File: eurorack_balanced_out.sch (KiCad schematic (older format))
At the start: 6 parts

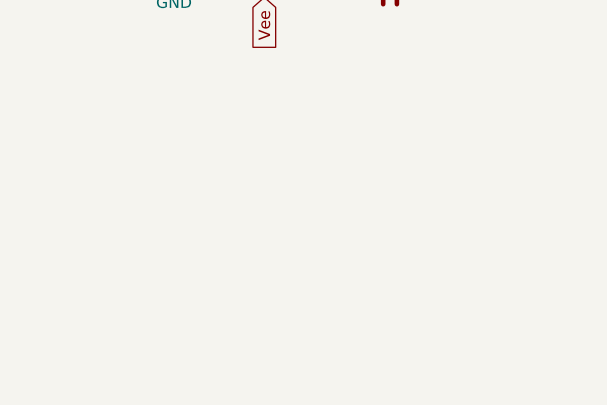
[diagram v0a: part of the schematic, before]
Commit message: add eurorack power connector + filtering
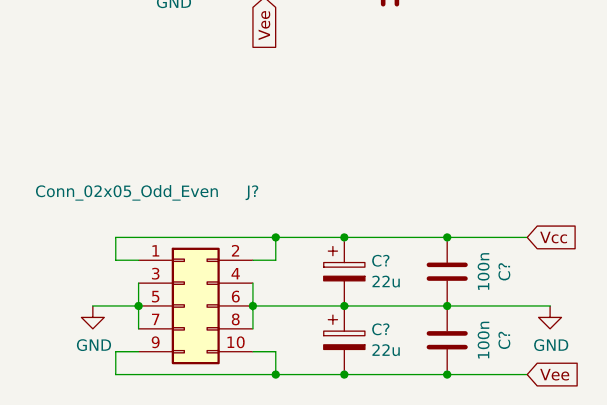
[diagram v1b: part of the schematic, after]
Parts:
- added C? (x2): 22u, Capacitor_SMD:CP_Elec_6.3x5.4, symbol Device:CP
- added C? (x2): 100n, Capacitor_SMD:C_0805_2012Metric_Pad1.15x1.40mm_HandSolder, symbol Device:C
- added J?: Conn_02x05_Odd_Even, symbol Connector_Generic:Conn_02x05_Odd_Even
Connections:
- net GND: now also C?.1, C?.1, C?.2, C?.2, J?.3 (Pin_3), J?.4 (Pin_4), J?.5 (Pin_5), J?.6 (Pin_6), J?.7 (Pin_7), J?.8 (Pin_8)
- net Vcc: now also C?.1, C?.2, J?.1 (Pin_1), J?.2 (Pin_2)
- net Vee: now also C?.1, C?.2, J?.10 (Pin_10), J?.9 (Pin_9)
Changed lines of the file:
@@
 Wire Wire Line
 	4400 3100 4600 3100
+$Comp
+L Connector_Generic:Conn_02x05_Odd_Even J?
+U 1 1 5EC6D021
+P 4450 4800
+F 0 "J?" H 4750 5300 50  0000 C CNN
+F 1 "Conn_02x05_Odd_Even" H 4200 5300 50  0000 C CNN
+F 2 "" H 4450 4800 50  0001 C CNN
+F 3 "~" H 4450 4800 50  0001 C CNN
+	1    4450 4800
+	1    0    0    -1
+$EndComp
+Wire Wire Line
+	4250 4900 4250 4800
+Connection ~ 4250 4800
+Wire Wire Line
+	4250 4800 4250 4700
+Wire Wire Line
+	4750 4700 4750 4800
+Connection ~ 4750 4800
+Wire Wire Line
+	4750 4800 4750 4900
+$Comp
+L power:GND #PWR?
+U 1 1 5EC6F187
+P 6050 4800
+F 0 "#PWR?" H 6050 4550 50  0001 C CNN
+F 1 "GND" H 6055 4627 50  0000 C CNN
+F 2 "" H 6050 4800 50  0001 C CNN
+F 3 "" H 6050 4800 50  0001 C CNN
+	1    6050 4800
+	1    0    0    -1
+$EndComp
+Wire Wire Line
+	4250 4800 4050 4800
+Wire Wire Line
+	4250 4600 4150 4600
+Wire Wire Line
+	4150 4600 4150 4500
+Wire Wire Line
+	4150 4500 4850 4500
+Wire Wire Line
+	4850 4500 4850 4600
+Wire Wire Line
+	4850 4600 4750 4600
+Wire Wire Line
+	4250 5000 4150 5000
+Wire Wire Line
+	4150 5000 4150 5100
+Wire Wire Line
+	4150 5100 4850 5100
+Wire Wire Line
+	4850 5100 4850 5000
+Wire Wire Line
+	4850 5000 4750 5000
+$Comp
+L Device:CP C?
+U 1 1 5EC72C83
+P 5150 4650
+F 0 "C?" H 5268 4696 50  0000 L CNN
+F 1 "22u" H 5268 4605 50  0000 L CNN
+F 2 "Capacitor_SMD:CP_Elec_6.3x5.4" H 5188 4500 50  0001 C CNN
+F 3 "~" H 5150 4650 50  0001 C CNN
+F 4 "647-UWT1E220MCL1B" H 5150 4650 50  0001 C CNN "Mouser"
+	1    5150 4650
+	1    0    0    -1
+$EndComp
+$Comp
+L Device:C C?
+U 1 1 5EC731D9
+P 5600 4650
+F 0 "C?" V 5348 4650 50  0000 C CNN
+F 1 "100n" V 5439 4650 50  0000 C CNN
+F 2 "Capacitor_SMD:C_0805_2012Metric_Pad1.15x1.40mm_HandSolder" H 5638 4500 50  0001 C CNN
+F 3 "~" H 5600 4650 50  0001 C CNN
+F 4 " 80-C0805C104K5RACLR" V 5600 4650 50  0001 C CNN "Mouser"
+	1    5600 4650
+	-1   0    0    1
+$EndComp
+Wire Wire Line
+	4850 4500 5150 4500
+Connection ~ 4850 4500
+Connection ~ 5150 4500
+Wire Wire Line
+	5150 4500 5600 4500
+Connection ~ 4850 5100
+Text GLabel 5950 5100 2    50   Input ~ 0
+Vee
+Text GLabel 5950 4500 2    50   Input ~ 0
+Vcc
+Wire Wire Line
+	5950 4500 5600 4500
+Connection ~ 5600 4500
+Connection ~ 5150 4800
+Wire Wire Line
+	5150 4800 5600 4800
+Connection ~ 5600 4800
+Wire Wire Line
+	5600 4800 6050 4800
+Wire Wire Line
+	4850 5100 5150 5100
+$Comp
+L Device:CP C?
+U 1 1 5EC7F6E5
+P 5150 4950
+F 0 "C?" H 5268 4996 50  0000 L CNN
+F 1 "22u" H 5268 4905 50  0000 L CNN
+F 2 "Capacitor_SMD:CP_Elec_6.3x5.4" H 5188 4800 50  0001 C CNN
+F 3 "~" H 5150 4950 50  0001 C CNN
+F 4 "647-UWT1E220MCL1B" H 5150 4950 50  0001 C CNN "Mouser"
+	1    5150 4950
+	1    0    0    -1
+$EndComp
+Connection ~ 5150 5100
+Wire Wire Line
+	4750 4800 5150 4800
+$Comp
+L power:GND #PWR?
+U 1 1 5EC7FEB8
+P 4050 4800
+F 0 "#PWR?" H 4050 4550 50  0001 C CNN
+F 1 "GND" H 4055 4627 50  0000 C CNN
+F 2 "" H 4050 4800 50  0001 C CNN
+F 3 "" H 4050 4800 50  0001 C CNN
+	1    4050 4800
+	1    0    0    -1
+$EndComp
+Wire Wire Line
+	5150 5100 5600 5100
+$Comp
+L Device:C C?
+U 1 1 5EC8D523
+P 5600 4950
+F 0 "C?" V 5348 4950 50  0000 C CNN
+F 1 "100n" V 5439 4950 50  0000 C CNN
+F 2 "Capacitor_SMD:C_0805_2012Metric_Pad1.15x1.40mm_HandSolder" H 5638 4800 50  0001 C CNN
+F 3 "~" H 5600 4950 50  0001 C CNN
+F 4 " 80-C0805C104K5RACLR" V 5600 4950 50  0001 C CNN "Mouser"
+	1    5600 4950
+	-1   0    0    1
+$EndComp
+Connection ~ 5600 5100
+Wire Wire Line
+	5600 5100 5950 5100
 $EndSCHEMATC

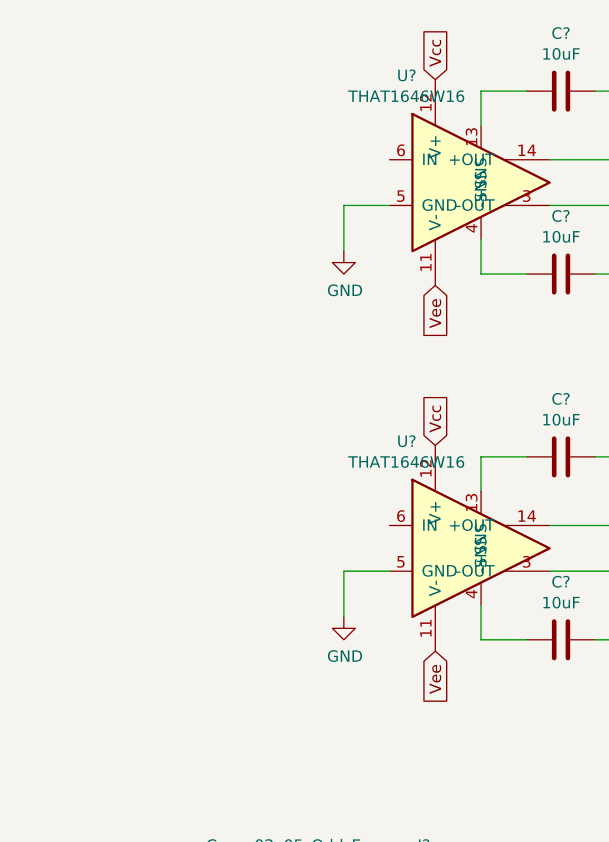
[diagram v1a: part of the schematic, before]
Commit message: add input connectors
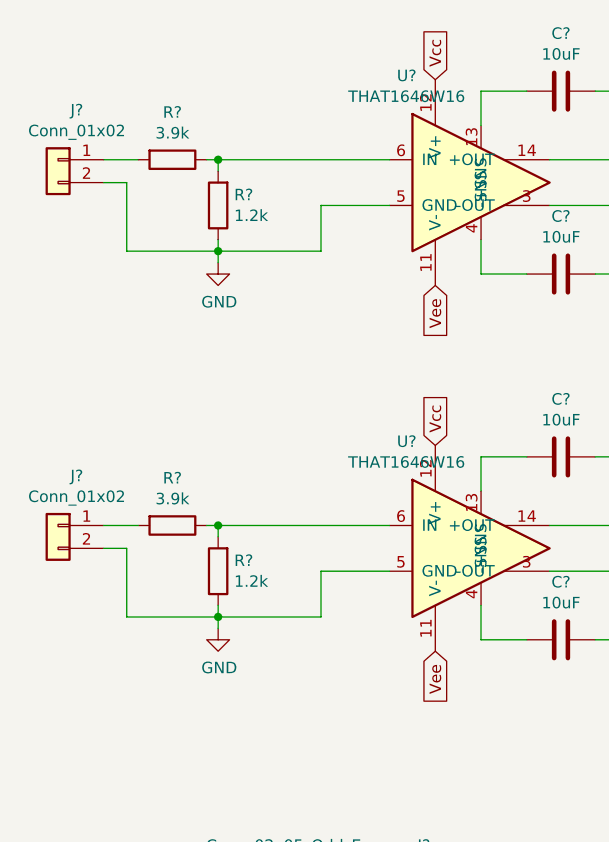
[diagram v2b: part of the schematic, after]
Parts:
- added J? (x2): Conn_01x02, symbol Connector_Generic:Conn_01x02
- added R? (x2): 3.9k, Resistor_SMD:R_0805_2012Metric_Pad1.15x1.40mm_HandSolder, symbol Device:R
- added R? (x2): 1.2k, Resistor_SMD:R_0805_2012Metric_Pad1.15x1.40mm_HandSolder, symbol Device:R
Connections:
- net GND: now also J?.2 (Pin_2), J?.2 (Pin_2), R?.1, R?.1
- net at U?.6 (IN): now also R?.1, R?.2 (x2)
- new net: J?.1 (Pin_1), R?.2 (x2)
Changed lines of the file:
@@
 L power:GND #PWR?
 U 1 1 5EC6D54F
-P 4400 1700
-F 0 "#PWR?" H 4400 1450 50  0001 C CNN
-F 1 "GND" H 4405 1527 50  0000 C CNN
-F 2 "" H 4400 1700 50  0001 C CNN
-F 3 "" H 4400 1700 50  0001 C CNN
-	1    4400 1700
-	1    0    0    -1
-$EndComp
-Wire Wire Line
-	4400 1700 4400 1500
-Wire Wire Line
-	4400 1500 4600 1500
+P 3850 1750
+F 0 "#PWR?" H 3850 1500 50  0001 C CNN
+F 1 "GND" H 3855 1577 50  0000 C CNN
+F 2 "" H 3850 1750 50  0001 C CNN
+F 3 "" H 3850 1750 50  0001 C CNN
+	1    3850 1750
+	1    0    0    -1
+$EndComp
 $Comp
 L patchut:THAT1646W16 U?
@@
 Vcc
 $Comp
-L power:GND #PWR?
-U 1 1 5EC6EB3D
-P 4400 3300
-F 0 "#PWR?" H 4400 3050 50  0001 C CNN
-F 1 "GND" H 4405 3127 50  0000 C CNN
-F 2 "" H 4400 3300 50  0001 C CNN
-F 3 "" H 4400 3300 50  0001 C CNN
-	1    4400 3300
-	1    0    0    -1
-$EndComp
-Wire Wire Line
-	4400 3300 4400 3100
-Wire Wire Line
-	4400 3100 4600 3100
-$Comp
 L Connector_Generic:Conn_02x05_Odd_Even J?
 U 1 1 5EC6D021
@@
 Wire Wire Line
 	5600 5100 5950 5100
+$Comp
+L Connector_Generic:Conn_01x02 J?
+U 1 1 5EC8DDA9
+P 3150 1300
+F 0 "J?" H 3068 1517 50  0000 C CNN
+F 1 "Conn_01x02" H 3068 1426 50  0000 C CNN
+F 2 "" H 3150 1300 50  0001 C CNN
+F 3 "~" H 3150 1300 50  0001 C CNN
+	1    3150 1300
+	-1   0    0    -1
+$EndComp
+$Comp
+L Device:R R?
+U 1 1 5EC8E9B6
+P 3650 1300
+F 0 "R?" V 3443 1300 50  0000 C CNN
+F 1 "3.9k" V 3534 1300 50  0000 C CNN
+F 2 "Resistor_SMD:R_0805_2012Metric_Pad1.15x1.40mm_HandSolder" V 3580 1300 50  0001 C CNN
+F 3 "~" H 3650 1300 50  0001 C CNN
+	1    3650 1300
+	0    1    1    0
+$EndComp
+Wire Wire Line
+	3500 1300 3350 1300
+Wire Wire Line
+	3800 1300 3850 1300
+Wire Wire Line
+	3850 1350 3850 1300
+Connection ~ 3850 1300
+Wire Wire Line
+	3850 1300 4600 1300
+Wire Wire Line
+	3850 1650 3850 1700
+Connection ~ 3850 1700
+Wire Wire Line
+	3850 1700 3850 1750
+Wire Wire Line
+	3350 1400 3450 1400
+Wire Wire Line
+	3450 1400 3450 1700
+Wire Wire Line
+	3450 1700 3850 1700
+Wire Wire Line
+	4600 1500 4300 1500
+Wire Wire Line
+	4300 1500 4300 1700
+Wire Wire Line
+	3850 1700 4300 1700
+$Comp
+L power:GND #PWR?
+U 1 1 5ECB48AD
+P 3850 3350
+F 0 "#PWR?" H 3850 3100 50  0001 C CNN
+F 1 "GND" H 3855 3177 50  0000 C CNN
+F 2 "" H 3850 3350 50  0001 C CNN
+F 3 "" H 3850 3350 50  0001 C CNN
+	1    3850 3350
+	1    0    0    -1
+$EndComp
+$Comp
+L Connector_Generic:Conn_01x02 J?
+U 1 1 5ECB48B3
+P 3150 2900
+F 0 "J?" H 3068 3117 50  0000 C CNN
+F 1 "Conn_01x02" H 3068 3026 50  0000 C CNN
+F 2 "" H 3150 2900 50  0001 C CNN
+F 3 "~" H 3150 2900 50  0001 C CNN
+	1    3150 2900
+	-1   0    0    -1
+$EndComp
+Wire Wire Line
+	3500 2900 3350 2900
+Wire Wire Line
+	3800 2900 3850 2900
+Wire Wire Line
+	3850 2950 3850 2900
+Connection ~ 3850 2900
+Wire Wire Line
+	3850 2900 4600 2900
+Wire Wire Line
+	3850 3250 3850 3300
+Connection ~ 3850 3300
+Wire Wire Line
+	3850 3300 3850 3350
+Wire Wire Line
+	3350 3000 3450 3000
+Wire Wire Line
+	3450 3000 3450 3300
+Wire Wire Line
+	3450 3300 3850 3300
+Wire Wire Line
+	3850 3300 4300 3300
+Wire Wire Line
+	4300 3300 4300 3100
+Wire Wire Line
+	4300 3100 4600 3100
+$Comp
+L Device:R R?
+U 1 1 5ECB87DC
+P 3850 1500
+F 0 "R?" H 3780 1454 50  0000 R CNN
+F 1 "1.2k" H 3780 1545 50  0000 R CNN
+F 2 "Resistor_SMD:R_0805_2012Metric_Pad1.15x1.40mm_HandSolder" V 3780 1500 50  0001 C CNN
+F 3 "~" H 3850 1500 50  0001 C CNN
+	1    3850 1500
+	-1   0    0    1
+$EndComp
+$Comp
+L Device:R R?
+U 1 1 5ECB902C
+P 3850 3100
+F 0 "R?" H 3780 3054 50  0000 R CNN
+F 1 "1.2k" H 3780 3145 50  0000 R CNN
+F 2 "Resistor_SMD:R_0805_2012Metric_Pad1.15x1.40mm_HandSolder" V 3780 3100 50  0001 C CNN
+F 3 "~" H 3850 3100 50  0001 C CNN
+	1    3850 3100
+	-1   0    0    1
+$EndComp
+$Comp
+L Device:R R?
+U 1 1 5ECB9314
+P 3650 2900
+F 0 "R?" V 3443 2900 50  0000 C CNN
+F 1 "3.9k" V 3534 2900 50  0000 C CNN
+F 2 "Resistor_SMD:R_0805_2012Metric_Pad1.15x1.40mm_HandSolder" V 3580 2900 50  0001 C CNN
+F 3 "~" H 3650 2900 50  0001 C CNN
+	1    3650 2900
+	0    1    1    0
+$EndComp
 $EndSCHEMATC

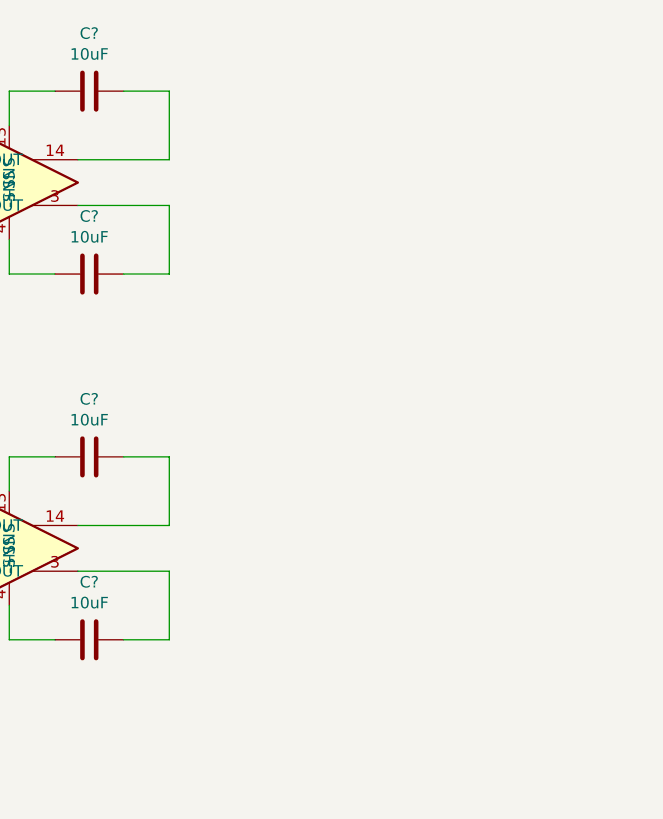
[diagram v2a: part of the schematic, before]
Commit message: add output jacks
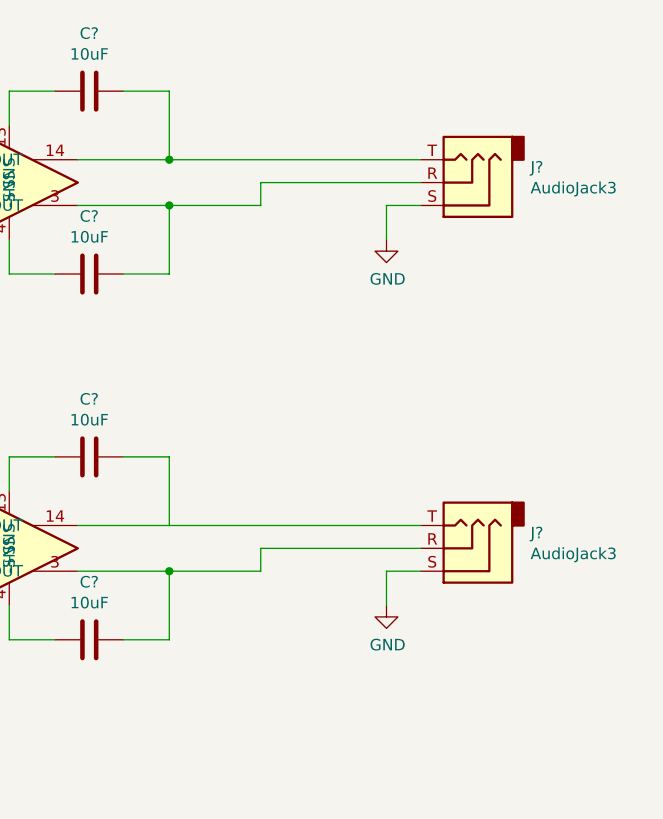
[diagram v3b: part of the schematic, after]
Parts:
- added J? (x2): AudioJack3, symbol Connector:AudioJack3
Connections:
- net GND: now also J?.S, J?.S
- net at C?.1, U?.14 (+OUT): now also J?.T (x2)
- net at C?.1, U?.3 (-OUT): now also J?.R (x2)
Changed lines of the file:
@@
 	0    1    1    0
 $EndComp
+$Comp
+L Connector:AudioJack3 J?
+U 1 1 5ECBA746
+P 7000 1400
+F 0 "J?" H 6720 1333 50  0000 R CNN
+F 1 "AudioJack3" H 6720 1424 50  0000 R CNN
+F 2 "" H 7000 1400 50  0001 C CNN
+F 3 "~" H 7000 1400 50  0001 C CNN
+	1    7000 1400
+	-1   0    0    1
+$EndComp
+Wire Wire Line
+	6800 1300 5700 1300
+Connection ~ 5700 1300
+Wire Wire Line
+	6800 1400 6100 1400
+Wire Wire Line
+	6100 1400 6100 1500
+Wire Wire Line
+	6100 1500 5700 1500
+Connection ~ 5700 1500
+$Comp
+L power:GND #PWR?
+U 1 1 5ECC7C45
+P 6650 1650
+F 0 "#PWR?" H 6650 1400 50  0001 C CNN
+F 1 "GND" H 6655 1477 50  0000 C CNN
+F 2 "" H 6650 1650 50  0001 C CNN
+F 3 "" H 6650 1650 50  0001 C CNN
+	1    6650 1650
+	1    0    0    -1
+$EndComp
+Wire Wire Line
+	6800 1500 6650 1500
+Wire Wire Line
+	6650 1500 6650 1650
+$Comp
+L Connector:AudioJack3 J?
+U 1 1 5ECCD754
+P 7000 3000
+F 0 "J?" H 6720 2933 50  0000 R CNN
+F 1 "AudioJack3" H 6720 3024 50  0000 R CNN
+F 2 "" H 7000 3000 50  0001 C CNN
+F 3 "~" H 7000 3000 50  0001 C CNN
+	1    7000 3000
+	-1   0    0    1
+$EndComp
+Wire Wire Line
+	6800 2900 5700 2900
+Wire Wire Line
+	6800 3000 6100 3000
+$Comp
+L power:GND #PWR?
+U 1 1 5ECCD75C
+P 6650 3250
+F 0 "#PWR?" H 6650 3000 50  0001 C CNN
+F 1 "GND" H 6655 3077 50  0000 C CNN
+F 2 "" H 6650 3250 50  0001 C CNN
+F 3 "" H 6650 3250 50  0001 C CNN
+	1    6650 3250
+	1    0    0    -1
+$EndComp
+Wire Wire Line
+	6800 3100 6650 3100
+Wire Wire Line
+	6650 3100 6650 3250
+Wire Wire Line
+	5700 3100 6100 3100
+Wire Wire Line
+	6100 3100 6100 3000
+Connection ~ 5700 3100
 $EndSCHEMATC

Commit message: add output footprint
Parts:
- removed J?: AudioJack3, symbol Connector:AudioJack3
- added J?: AudioJack3, Connector_Audio:Jack_6.35mm_Neutrik_NJ3FD-V_Vertical, symbol Connector:AudioJack3
- J?: footprint (none) -> Connector_Audio:Jack_6.35mm_Neutrik_NJ3FD-V_Vertical
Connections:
- net GND: now also J?.S
- net at C?.1, U?.14 (+OUT): now also J?.T
- net at C?.1, U?.3 (-OUT): now also J?.R
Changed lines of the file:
@@
 	0    1    1    0
-$EndComp
-$Comp
-L Connector:AudioJack3 J?
-U 1 1 5ECBA746
-P 7000 1400
-F 0 "J?" H 6720 1333 50  0000 R CNN
-F 1 "AudioJack3" H 6720 1424 50  0000 R CNN
-F 2 "" H 7000 1400 50  0001 C CNN
-F 3 "~" H 7000 1400 50  0001 C CNN
-	1    7000 1400
-	-1   0    0    1
 $EndComp
 Wire Wire Line
@@
 F 0 "J?" H 6720 2933 50  0000 R CNN
 F 1 "AudioJack3" H 6720 3024 50  0000 R CNN
-F 2 "" H 7000 3000 50  0001 C CNN
+F 2 "Connector_Audio:Jack_6.35mm_Neutrik_NJ3FD-V_Vertical" H 7000 3000 50  0001 C CNN
 F 3 "~" H 7000 3000 50  0001 C CNN
 	1    7000 3000
@@
 	6100 3100 6100 3000
 Connection ~ 5700 3100
+$Comp
+L Connector:AudioJack3 J?
+U 1 1 5EC84302
+P 7000 1400
+F 0 "J?" H 6720 1333 50  0000 R CNN
+F 1 "AudioJack3" H 6720 1424 50  0000 R CNN
+F 2 "Connector_Audio:Jack_6.35mm_Neutrik_NJ3FD-V_Vertical" H 7000 1400 50  0001 C CNN
+F 3 "~" H 7000 1400 50  0001 C CNN
+	1    7000 1400
+	-1   0    0    1
+$EndComp
 $EndSCHEMATC
